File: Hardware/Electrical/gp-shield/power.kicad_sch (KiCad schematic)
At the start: 30 parts, among them J1 XT60/TERM2, J2 XT60/TERM2, Q1 Q_PMOS_GDS, SW1 SW_SPDT, U1 NCP1117-5.0_SOT223, U2 LM4040DBZ-2.5, U4 LM397

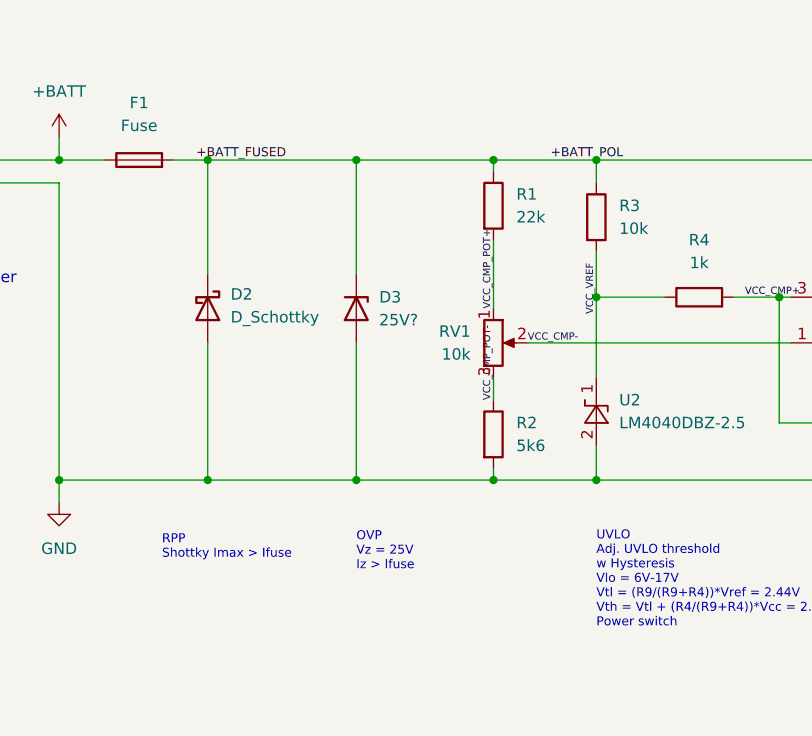
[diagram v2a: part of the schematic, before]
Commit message: Updated footprints and PCB layout
Updated reverse polarity and overvoltage to use bidirectional TVS diode
Changed footprint of TVS diode
Changed footprint of fuse to proper 5x20mm fuse holder
Changed footprint of PMOS high side switch to DPAK
Updated layout with Vreg on backside
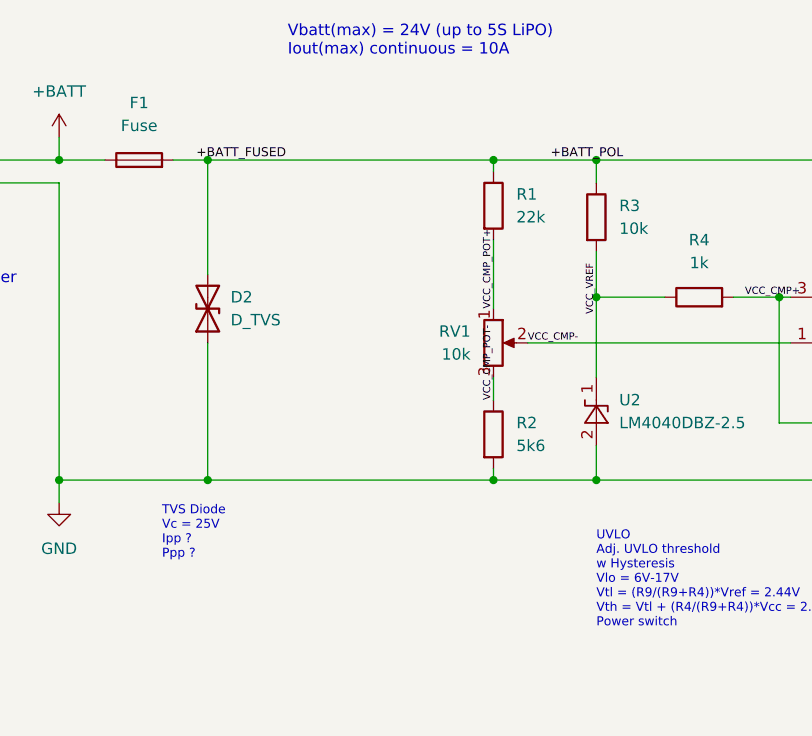
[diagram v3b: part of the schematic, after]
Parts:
- removed D2: D_Schottky, Diode_SMD:D_0805_2012Metric_Pad1.15x1.40mm_HandSolder, symbol Device:D_Schottky
- removed D3: 25V?, Diode_SMD:D_0805_2012Metric_Pad1.15x1.40mm_HandSolder, symbol Device:D_Zener
- added D2: D_TVS, Diode_SMD:D_SMA, symbol Device:D_TVS
- F1: footprint Fuse:Fuse_Littelfuse-LVR100 -> Fuse:Fuseholder_Littelfuse_445_030_series_5x20mm
- Q1: footprint Package_TO_SOT_SMD:SOT-23 -> Package_TO_SOT_SMD:TO-252-3_TabPin2
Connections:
- net +BATT_FUSED: now also D2.2 (A2)
- net GND: now also D2.1 (A1)
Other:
- note added: "TVS Diode Vc = 25V Ipp ? Ppp ?"
- note added: "Vbatt(max) = 24V (up to 5S LiPO) Iout(max) continuous = 10A"
- note removed: "OVP Vz = 25V Iz > Ifuse"
- note removed: "RPP Shottky Imax > Ifuse"
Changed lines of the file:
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@@
   (junction (at 95.25 67.31) (diameter 0) (color 0 0 0 0)
   )
-  (junction (at 68.58 67.31) (diameter 0) (color 0 0 0 0)
-  )
   (junction (at 105.41 109.22) (diameter 0) (color 0 0 0 0)
   )
@@
   )
   (junction (at 59.69 109.22) (diameter 0) (color 0 0 0 0)
-  )
-  (junction (at 68.58 31.75) (diameter 0) (color 0 0 0 0)
   )
   (junction (at 115.57 46.99) (diameter 0) (color 0 0 0 0)
@@
     (stroke (width 0) (type default) (color 0 0 0 0))
   )
-  (wire (pts (xy 52.07 67.31) (xy 68.58 67.31))
-    (stroke (width 0) (type default) (color 0 0 0 0))
-  )
   (wire (pts (xy 64.77 119.38) (xy 64.77 121.92))
     (stroke (width 0) (type default) (color 0 0 0 0))
@@
     (stroke (width 0) (type default) (color 0 0 0 0))
   )
-  (wire (pts (xy 52.07 31.75) (xy 68.58 31.75))
+  (wire (pts (xy 52.07 31.75) (xy 83.82 31.75))
     (stroke (width 0) (type default) (color 0 0 0 0))
   )
@@
     (stroke (width 0) (type default) (color 0 0 0 0))
   )
-  (wire (pts (xy 68.58 31.75) (xy 83.82 31.75))
-    (stroke (width 0) (type default) (color 0 0 0 0))
-  )
   (wire (pts (xy 26.67 34.29) (xy 35.56 34.29))
     (stroke (width 0) (type default) (color 0 0 0 0))
@@
     (stroke (width 0) (type default) (color 0 0 0 0))
   )
-  (wire (pts (xy 68.58 67.31) (xy 83.82 67.31))
+  (wire (pts (xy 52.07 67.31) (xy 83.82 67.31))
     (stroke (width 0) (type default) (color 0 0 0 0))
   )
@@
     (stroke (width 0) (type default) (color 0 0 0 0))
   )
-  (wire (pts (xy 68.58 52.07) (xy 68.58 67.31))
-    (stroke (width 0) (type default) (color 0 0 0 0))
-  )
   (wire (pts (xy 90.17 121.92) (xy 78.74 121.92))
     (stroke (width 0) (type default) (color 0 0 0 0))
@@
     (stroke (width 0) (type default) (color 0 0 0 0))
   )
-  (wire (pts (xy 68.58 31.75) (xy 68.58 44.45))
-    (stroke (width 0) (type default) (color 0 0 0 0))
-  )
   (wire (pts (xy 95.25 31.75) (xy 95.25 34.29))
     (stroke (width 0) (type default) (color 0 0 0 0))
@@
   (wire (pts (xy 111.76 109.22) (xy 105.41 109.22))
     (stroke (width 0) (type default) (color 0 0 0 0))
-  )
-  (text "OVP\nVz = 25V\nIz > Ifuse" (at 68.58 77.47 0)
-    (effects (font (size 1 1)) (justify left bottom))
   )
   (text "XT60\n0.2\" Terminal Port\n0.2\" stacking header" (at 12.7 45.72 0)
@@
     (effects (font (size 1.27 1.27)) (justify left bottom))
   )
+  (text "Vbatt(max) = 24V (up to 5S LiPO)\nIout(max) continuous = 10A"
+    (at 60.96 20.32 0)
+    (effects (font (size 1.27 1.27)) (justify left bottom))
+  )
   (text "Jumper for connection of 5V to arduino." (at 229.87 128.27 0)
     (effects (font (size 1.27 1.27)) (justify left bottom))
   )
-  (text "RPP\nShottky Imax > Ifuse" (at 46.99 76.2 0)
+  (text "TVS Diode\nVc = 25V\nIpp ?\nPpp ?" (at 46.99 76.2 0)
     (effects (font (size 1 1)) (justify left bottom))
   )
@@
     (property "Reference" "Q1" (id 0) (at 167.64 24.13 90))
     (property "Value" "Q_PMOS_GDS" (id 1) (at 167.64 26.67 90))
-    (property "Footprint" "Package_TO_SOT_SMD:SOT-23" (id 2) (at 170.18 29.21 0)
+    (property "Footprint" "Package_TO_SOT_SMD:TO-252-3_TabPin2" (id 2) (at 170.18 29.21 0)
       (effects (font (size 1.27 1.27)) hide)
     )
@@
     )
     (property "Datasheet" "~" (id 3) (at 95.25 38.1 0)
-      (effects (font (size 1.27 1.27)) hide)
-    )
-    (pin "1")
-    (pin "2")
-  )
-  (symbol (lib_id "Device:D_Schottky") (at 52.07 48.26 270) (unit 1)
-    (in_bom yes) (on_board yes) (fields_autoplaced)
-    (property "Reference" "D2" (id 0) (at 54.61 46.6724 90)
-      (effects (font (size 1.27 1.27)) (justify left))
-    )
-    (property "Value" "D_Schottky" (id 1) (at 54.61 49.2124 90)
-      (effects (font (size 1.27 1.27)) (justify left))
-    )
-    (property "Footprint" "Diode_SMD:D_0805_2012Metric_Pad1.15x1.40mm_HandSolder" (id 2) (at 52.07 48.26 0)
-      (effects (font (size 1.27 1.27)) hide)
-    )
-    (property "Datasheet" "~" (id 3) (at 52.07 48.26 0)
       (effects (font (size 1.27 1.27)) hide)
     )
@@
     (pin "5")
   )
+  (symbol (lib_id "Device:D_TVS") (at 52.07 48.26 90) (unit 1)
+    (in_bom yes) (on_board yes) (fields_autoplaced)
+    (property "Reference" "D2" (id 0) (at 54.61 46.9899 90)
+      (effects (font (size 1.27 1.27)) (justify right))
+    )
+    (property "Value" "D_TVS" (id 1) (at 54.61 49.5299 90)
+      (effects (font (size 1.27 1.27)) (justify right))
+    )
+    (property "Footprint" "Diode_SMD:D_SMA" (id 2) (at 52.07 48.26 0)
+      (effects (font (size 1.27 1.27)) hide)
+    )
+    (property "Datasheet" "~" (id 3) (at 52.07 48.26 0)
+      (effects (font (size 1.27 1.27)) hide)
+    )
+    (pin "1")
+    (pin "2")
+  )
   (symbol (lib_id "power:PWR_FLAG") (at 121.92 31.75 0) (unit 1)
     (in_bom yes) (on_board yes) (fields_autoplaced)
@@
     (property "Reference" "F1" (id 0) (at 44.45 25.4 90))
     (property "Value" "Fuse" (id 1) (at 44.45 27.94 90))
-    (property "Footprint" "Fuse:Fuse_Littelfuse-LVR100" (id 2) (at 44.45 33.528 90)
+    (property "Footprint" "Fuse:Fuseholder_Littelfuse_445_030_series_5x20mm" (id 2) (at 44.45 33.528 90)
       (effects (font (size 1.27 1.27)) hide)
     )
@@
       (effects (font (size 1.27 1.27)) hide)
     )
-    (pin "1")
-    (pin "2")
-  )
-  (symbol (lib_id "Device:D_Zener") (at 68.58 48.26 270) (unit 1)
-    (in_bom yes) (on_board yes) (fields_autoplaced)
-    (property "Reference" "D3" (id 0) (at 71.12 46.9899 90)
-      (effects (font (size 1.27 1.27)) (justify left))
-    )
-    (property "Value" "25V?" (id 1) (at 71.12 49.5299 90)
-      (effects (font (size 1.27 1.27)) (justify left))
-    )
-    (property "Footprint" "Diode_SMD:D_0805_2012Metric_Pad1.15x1.40mm_HandSolder" (id 2) (at 68.58 48.26 0)
-      (effects (font (size 1.27 1.27)) hide)
-    )
-    (property "Datasheet" "~" (id 3) (at 68.58 48.26 0)
-      (effects (font (size 1.27 1.27)) hide)
-    )

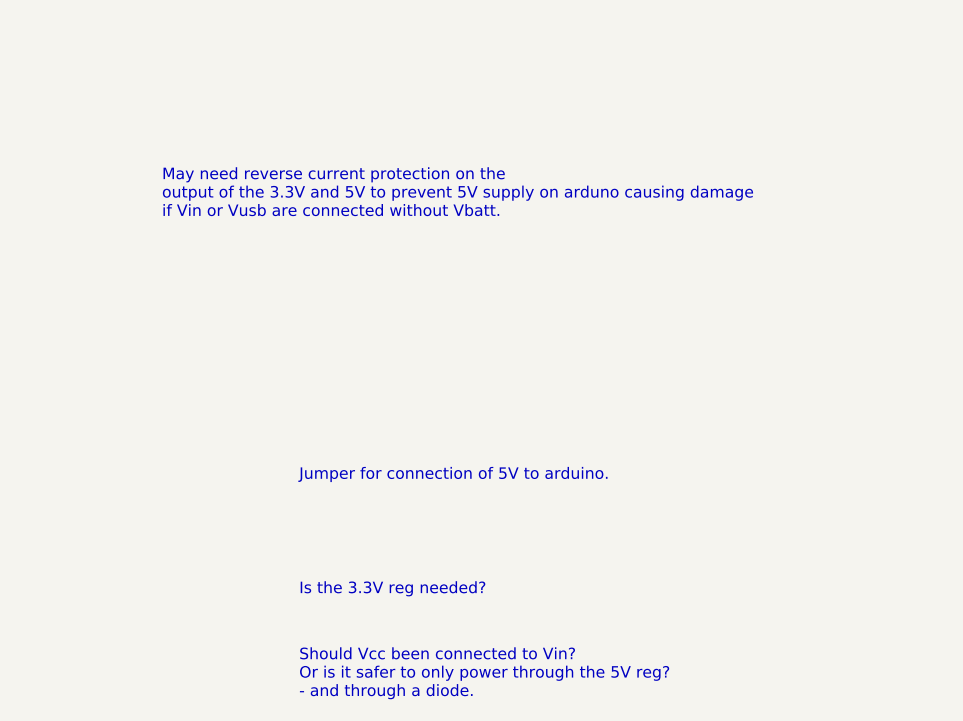
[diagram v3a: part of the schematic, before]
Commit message: Minor cosmetic imporvements
title block and colour theme
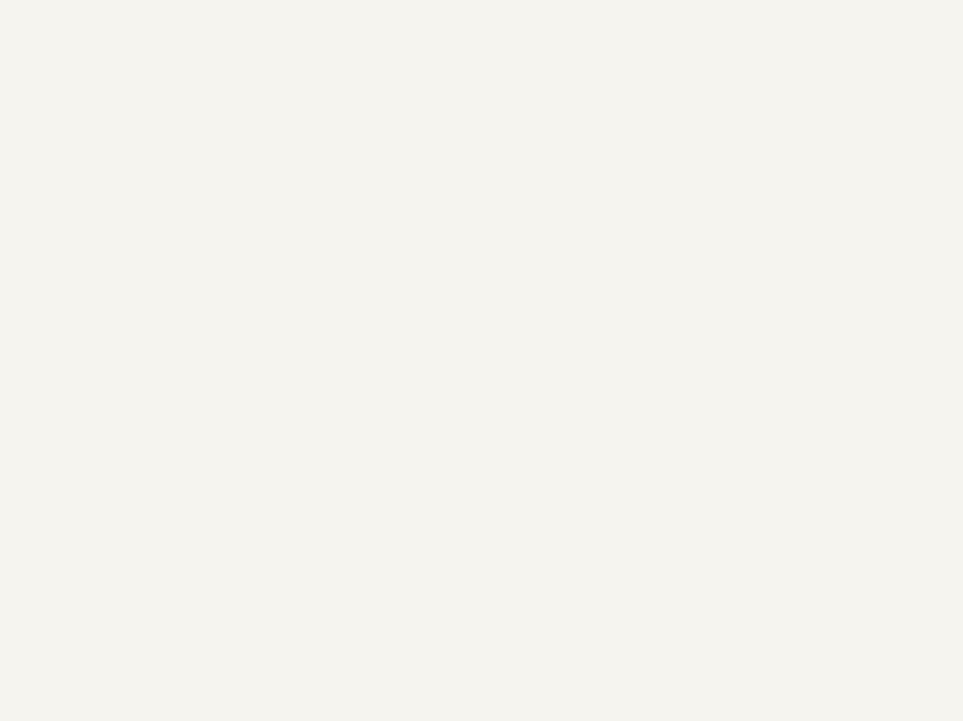
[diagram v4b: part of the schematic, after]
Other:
- note removed: "Is the 3.3V reg needed?"
- note removed: "Jumper for connection of 5V to arduino."
- note removed: "May need reverse current protection on the output of the 3.3V and 5V to prevent 5V supply on arduno causing damage if Vin or Vusb are connected without Vbatt."
- note removed: "Should Vcc been connected to Vin? Or is it safer to only power through the 5V reg? - and through a diode."
- company: (none) -> University of Tasmania
- title: (none) -> gp-shield Power Supply
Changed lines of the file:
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@@
 (kicad_sch (version 20211123) (generator eeschema)
   (paper "A4")
+  (title_block
+    (title "gp-shield Power Supply")
+    (date "2022-12-01")
+    (rev "1")
+    (company "University of Tasmania")
+  )
   (junction (at 35.56 67.31) (diameter 0) (color 0 0 0 0)
   )
@@
     (effects (font (size 1.27 1.27)) (justify left bottom))
   )
-  (text "Is the 3.3V reg needed?" (at 229.87 140.97 0)
-    (effects (font (size 1.27 1.27)) (justify left bottom))
-  )
   (text "Dual footprint\nDIP switch\n2.54mm header." (at 149.86 74.93 0)
     (effects (font (size 1.27 1.27)) (justify left bottom))
   )
   (text "XT60\n0.2\" Terminal Port\n0.2\" stacking header" (at 262.89 53.34 0)
-    (effects (font (size 1.27 1.27)) (justify left bottom))
-  )
-  (text "Should Vcc been connected to Vin?\nOr is it safer to only power through the 5V reg?\n- and through a diode."
-    (at 229.87 152.4 0)
     (effects (font (size 1.27 1.27)) (justify left bottom))
   )
@@
     (effects (font (size 1 1)) (justify left bottom))
   )
-  (text "May need reverse current protection on the\noutput of the 3.3V and 5V to prevent 5V supply on arduno causing damage\nif Vin or Vusb are connected without Vbatt."
-    (at 214.63 99.06 0)
-    (effects (font (size 1.27 1.27)) (justify left bottom))
-  )
   (text "Vbatt(max) = 24V (up to 5S LiPO)\nIout(max) continuous = 10A"
     (at 60.96 20.32 0)
     (effects (font (size 1.27 1.27)) (justify left bottom))
   )
-  (text "Jumper for connection of 5V to arduino." (at 229.87 128.27 0)
-    (effects (font (size 1.27 1.27)) (justify left bottom))
-  )

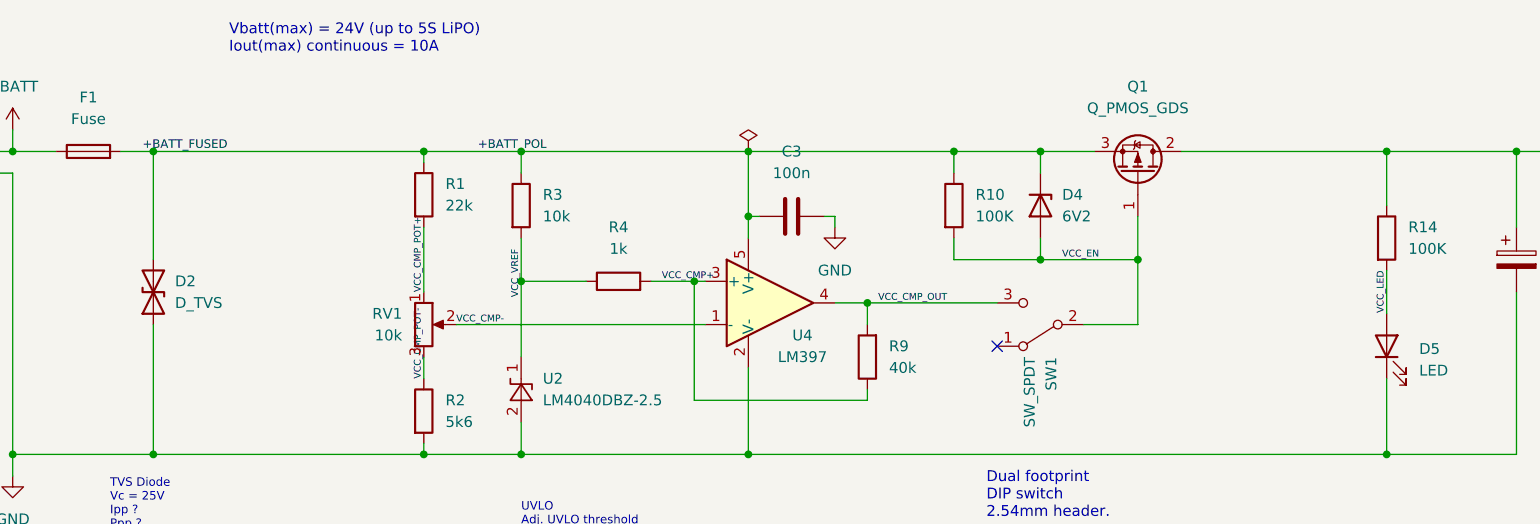
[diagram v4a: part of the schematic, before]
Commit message: Added test points for key power signals
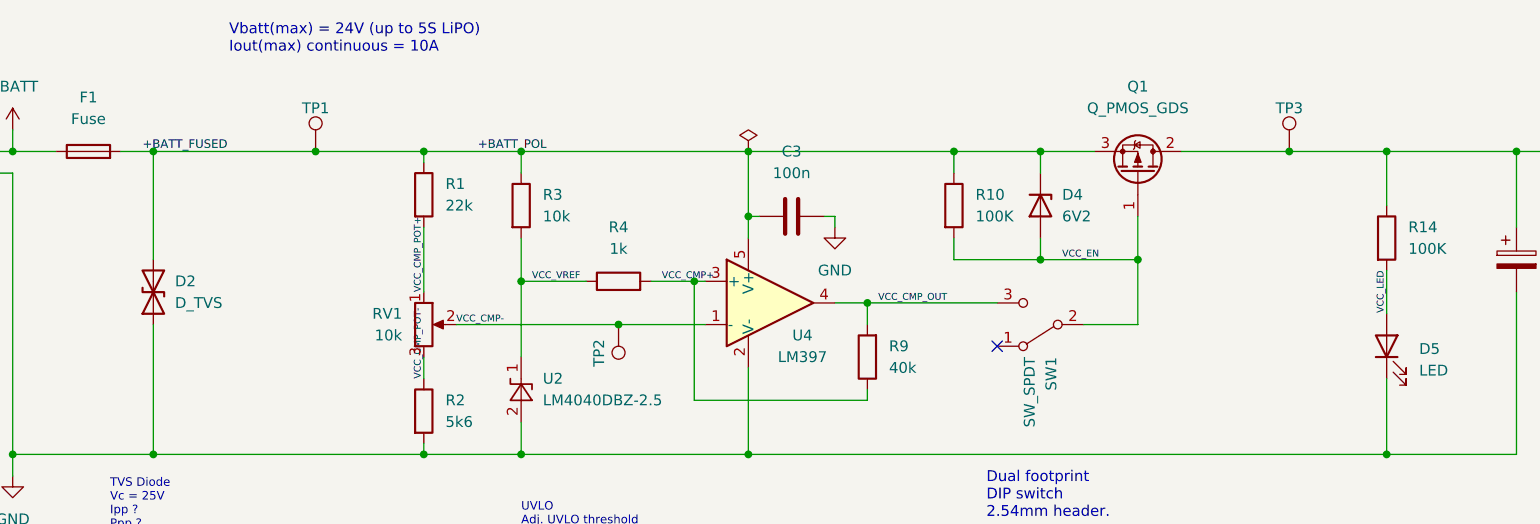
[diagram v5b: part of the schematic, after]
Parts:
- added TP1, TP2, TP3: TestPoint, TestPoint:TestPoint_THTPad_D2.0mm_Drill1.0mm, symbol Connector:TestPoint
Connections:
- net +BATT_FUSED: now also TP1.1
- net VCC: now also TP3.1
- net VCC_CMP-: now also TP2.1
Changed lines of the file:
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@@
   (junction (at 64.77 109.22) (diameter 0) (color 0 0 0 0)
   )
+  (junction (at 71.12 31.75) (diameter 0) (color 0 0 0 0)
+  )
   (junction (at 90.17 109.22) (diameter 0) (color 0 0 0 0)
   )
   (junction (at 83.82 67.31) (diameter 0) (color 0 0 0 0)
   )
+  (junction (at 106.68 52.07) (diameter 0) (color 0 0 0 0)
+  )
   (junction (at 59.69 109.22) (diameter 0) (color 0 0 0 0)
+  )
+  (junction (at 185.42 31.75) (diameter 0) (color 0 0 0 0)
   )
   (junction (at 115.57 46.99) (diameter 0) (color 0 0 0 0)
@@
     (stroke (width 0) (type default) (color 0 0 0 0))
   )
+  (wire (pts (xy 185.42 31.75) (xy 196.85 31.75))
+    (stroke (width 0) (type default) (color 0 0 0 0))
+  )
   (wire (pts (xy 64.77 109.22) (xy 71.12 109.22))
     (stroke (width 0) (type default) (color 0 0 0 0))
@@
     (stroke (width 0) (type default) (color 0 0 0 0))
   )
+  (wire (pts (xy 71.12 31.75) (xy 83.82 31.75))
+    (stroke (width 0) (type default) (color 0 0 0 0))
+  )
   (wire (pts (xy 196.85 45.72) (xy 196.85 50.8))
     (stroke (width 0) (type default) (color 0 0 0 0))
@@
     (stroke (width 0) (type default) (color 0 0 0 0))
   )
-  (wire (pts (xy 52.07 31.75) (xy 83.82 31.75))
+  (wire (pts (xy 52.07 31.75) (xy 71.12 31.75))
     (stroke (width 0) (type default) (color 0 0 0 0))
   )
@@
     (stroke (width 0) (type default) (color 0 0 0 0))
   )
-  (wire (pts (xy 172.72 31.75) (xy 196.85 31.75))
+  (wire (pts (xy 172.72 31.75) (xy 185.42 31.75))
     (stroke (width 0) (type default) (color 0 0 0 0))
   )
@@
     (stroke (width 0) (type default) (color 0 0 0 0))
   )
-  (wire (pts (xy 87.63 52.07) (xy 116.84 52.07))
+  (wire (pts (xy 87.63 52.07) (xy 106.68 52.07))
     (stroke (width 0) (type default) (color 0 0 0 0))
   )
@@
   )
   (wire (pts (xy 219.71 31.75) (xy 242.57 31.75))
+    (stroke (width 0) (type default) (color 0 0 0 0))
+  )
+  (wire (pts (xy 106.68 52.07) (xy 116.84 52.07))
     (stroke (width 0) (type default) (color 0 0 0 0))
   )
@@
     (effects (font (size 1 1)) (justify left bottom))
   )
-  (label "VCC_VREF" (at 95.25 43.18 270)
-    (effects (font (size 0.8 0.8)) (justify right bottom))
+  (label "VCC_VREF" (at 96.52 46.99 0)
+    (effects (font (size 0.8 0.8)) (justify left bottom))
   )
   (symbol (lib_id "power:PWR_FLAG") (at 219.71 31.75 180) (unit 1)
@@
     (pin "5")
   )
+  (symbol (lib_id "Connector:TestPoint") (at 71.12 31.75 0) (unit 1)
+    (in_bom no) (on_board yes)
+    (property "Reference" "TP1" (id 0) (at 71.12 26.67 0))
+    (property "Value" "TestPoint" (id 1) (at 74.93 28.448 90)
+      (effects (font (size 1.27 1.27)) hide)
+    )
+    (property "Footprint" "TestPoint:TestPoint_THTPad_D2.0mm_Drill1.0mm" (id 2) (at 76.2 31.75 0)
+      (effects (font (size 1.27 1.27)) hide)
+    )
+    (property "Datasheet" "~" (id 3) (at 76.2 31.75 0)
+      (effects (font (size 1.27 1.27)) hide)
+    )
+    (pin "1")
+  )
   (symbol (lib_id "Device:D_TVS") (at 52.07 48.26 90) (unit 1)
     (in_bom yes) (on_board yes) (fields_autoplaced)
@@
     (pin "2")
   )
+  (symbol (lib_id "Connector:TestPoint") (at 185.42 31.75 0) (unit 1)
+    (in_bom no) (on_board yes)
+    (property "Reference" "TP3" (id 0) (at 185.42 26.67 0))
+    (property "Value" "TestPoint" (id 1) (at 189.23 28.448 90)
+      (effects (font (size 1.27 1.27)) hide)
+    )
+    (property "Footprint" "TestPoint:TestPoint_THTPad_D2.0mm_Drill1.0mm" (id 2) (at 190.5 31.75 0)
+      (effects (font (size 1.27 1.27)) hide)
+    )
+    (property "Datasheet" "~" (id 3) (at 190.5 31.75 0)
+      (effects (font (size 1.27 1.27)) hide)
+    )
+    (pin "1")
+  )
+  (symbol (lib_id "Connector:TestPoint") (at 106.68 52.07 180) (unit 1)
+    (in_bom no) (on_board yes)
+    (property "Reference" "TP2" (id 0) (at 104.3967 55.409 90))
+    (property "Value" "TestPoint" (id 1) (at 102.87 55.372 90)
+      (effects (font (size 1.27 1.27)) hide)
+    )
+    (property "Footprint" "TestPoint:TestPoint_THTPad_D2.0mm_Drill1.0mm" (id 2) (at 101.6 52.07 0)
+      (effects (font (size 1.27 1.27)) hide)
+    )
+    (property "Datasheet" "~" (id 3) (at 101.6 52.07 0)
+      (effects (font (size 1.27 1.27)) hide)
+    )
+    (pin "1")
+  )
   (symbol (lib_id "Device:Fuse") (at 44.45 31.75 90) (unit 1)
